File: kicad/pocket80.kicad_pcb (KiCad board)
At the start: 4 copper layers, 68.6 x 107.3 mm, 138 parts, among them J1 USB_C_Receptacle_USB2.0_14P, J2 Conn_02x10_Odd_Even, J3 Conn_01x02, Q1 IRLML6402, Q2 BC847, SW1 F1, SW10 4, SW11 9, SW12 5, SW13 A, SW14 6, SW15 B, SW16 7, SW17 0, SW18 INC, SW19 1, SW2 F2, SW20 DEC, SW21 2, SW22 SEL, SW23 3, SW24 GO!, SW25 SW_Push_DPDT, SW26 RESET, SW3 F3, SW4 F4, SW5 C, SW6 D, SW7 E, SW8 F, SW9 8, U1 Z80CPU, U10 74HC00, U11 74HC138, U12 CH340N, U13 TP4056-42-ESOP8, U14 SX1308, U15 LM393, U16 74HC74, U17 28C256, U2 74HC244, U3 Z80 PIO, U4 Z80 SIO3, U5 Z80 CTC, U6 NE555D, U7 74HC04, U8 62256, U9 24C512, Y1 3.6864M

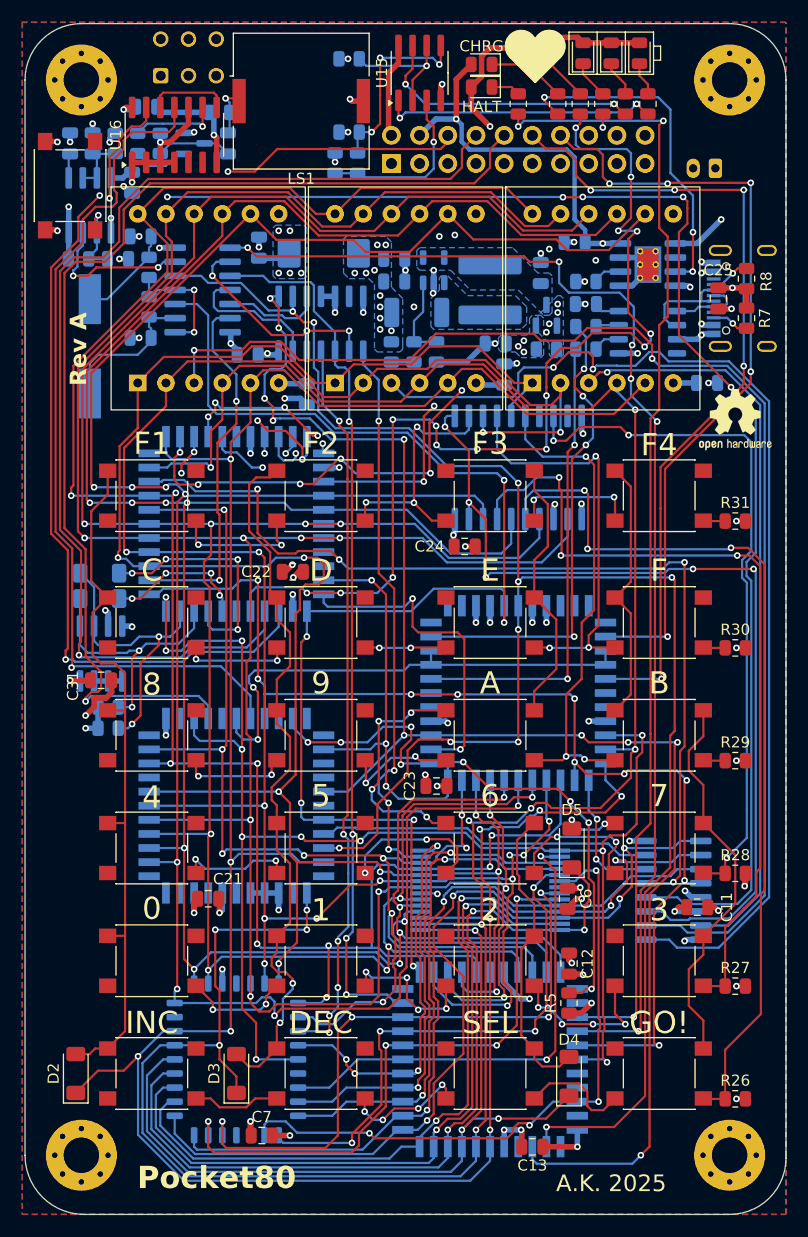
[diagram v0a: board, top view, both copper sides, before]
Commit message: HW: Fix slight mounting hole offset
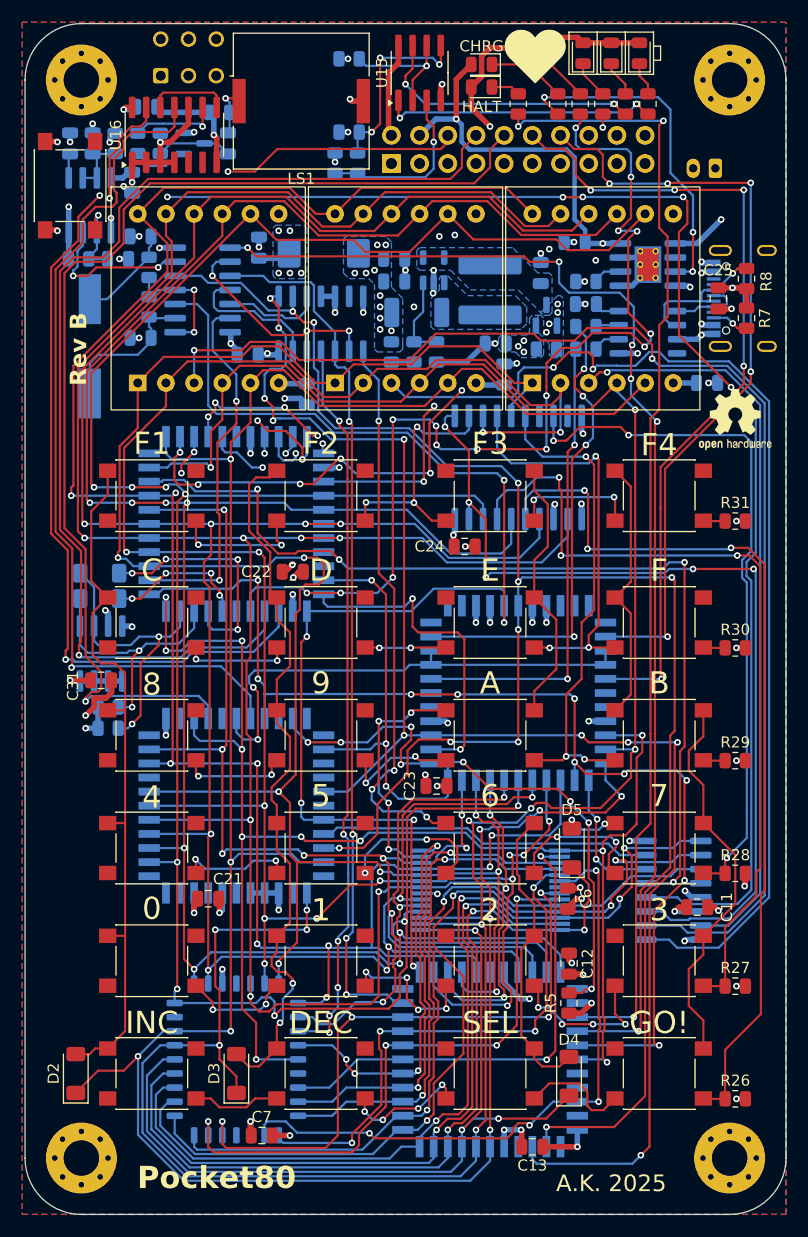
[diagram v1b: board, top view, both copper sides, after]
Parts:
- moved H3 0.25 mm to (160.0, 137.4)
- moved H4 0.25 mm to (101.6, 137.4)
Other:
- outline, holes or cut-outs redrawn
- board text added: "Rev B"
- board text removed: "Rev A"
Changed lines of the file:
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@@
 		(title "Pocket80")
 		(date "2025-10-19")
-		(rev "A")
+		(rev "B")
 		(company "A.K.")
 	)
@@
 	(footprint "MountingHole:MountingHole_3.2mm_M3_Pad_Via"
 		(layer "F.Cu")
-		(at 101.6 137.16)
+		(at 101.6 137.414)
 		(descr "Mounting Hole 3.2mm, M3")
 		(tags "mounting hole 3.2mm m3")
@@
 	(footprint "MountingHole:MountingHole_3.2mm_M3_Pad_Via"
 		(layer "F.Cu")
-		(at 160.02 137.16)
+		(at 160.02 137.414)
 		(descr "Mounting Hole 3.2mm, M3")
 		(tags "mounting hole 3.2mm m3")
@@
 	)
 	(gr_arc
-		(start 101.854 142.494)
-		(mid 98.082292 140.931708)
-		(end 96.52 137.16)
+		(start 101.6 142.494)
+		(mid 98.007898 141.006102)
+		(end 96.52 137.414)
 		(stroke
 			(width 0.05)
@@
 	)
 	(gr_line
-		(start 96.52 137.16)
+		(start 96.52 137.414)
 		(end 96.52 40.259)
 		(stroke
@@
 		(layer "Edge.Cuts")
 	)
-	(gr_line
-		(start 160.019998 142.494)
-		(end 101.854 142.494)
+	(gr_arc
+		(start 165.1 137.414)
+		(mid 163.612102 141.006102)
+		(end 160.02 142.494)
 		(stroke
 			(width 0.05)
@@
 		(layer "Edge.Cuts")
 	)
-	(gr_arc
-		(start 96.52 40.259)
-		(mid 98.007898 36.666898)
-		(end 101.6 35.179)
+	(gr_line
+		(start 160.019998 142.494)
+		(end 101.6 142.494)
 		(stroke
 			(width 0.05)
@@
 	)
 	(gr_arc
-		(start 165.099998 137.414)
-		(mid 163.6121 141.006102)
-		(end 160.019998 142.494)
+		(start 96.52 40.259)
+		(mid 98.007898 36.666898)
+		(end 101.6 35.179)
 		(stroke
 			(width 0.05)
@@
 		)
 	)
-	(gr_text "Rev A"
+	(gr_text "Rev B"
 		(at 101.346 64.516 90)
 		(layer "F.SilkS")

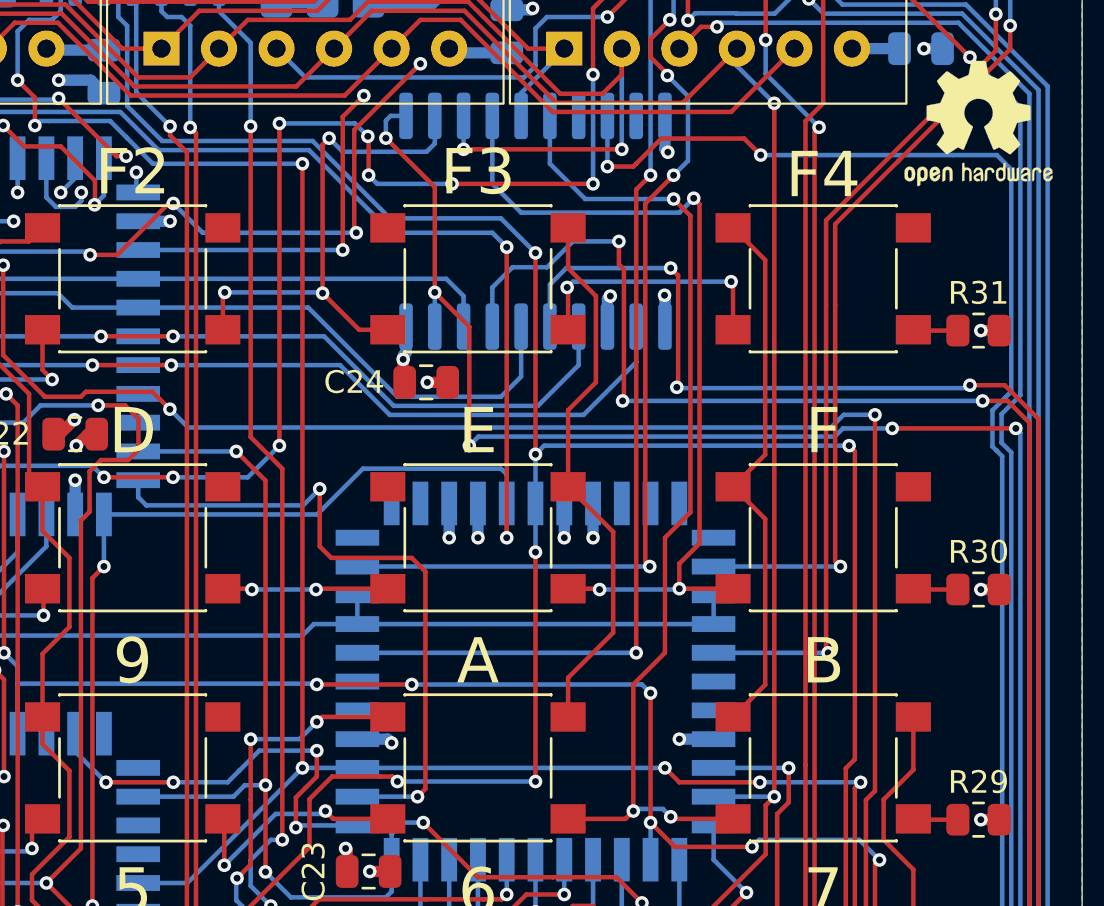
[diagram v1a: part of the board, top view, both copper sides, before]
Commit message: HW: Add pull-ups to the expansion slot inputs
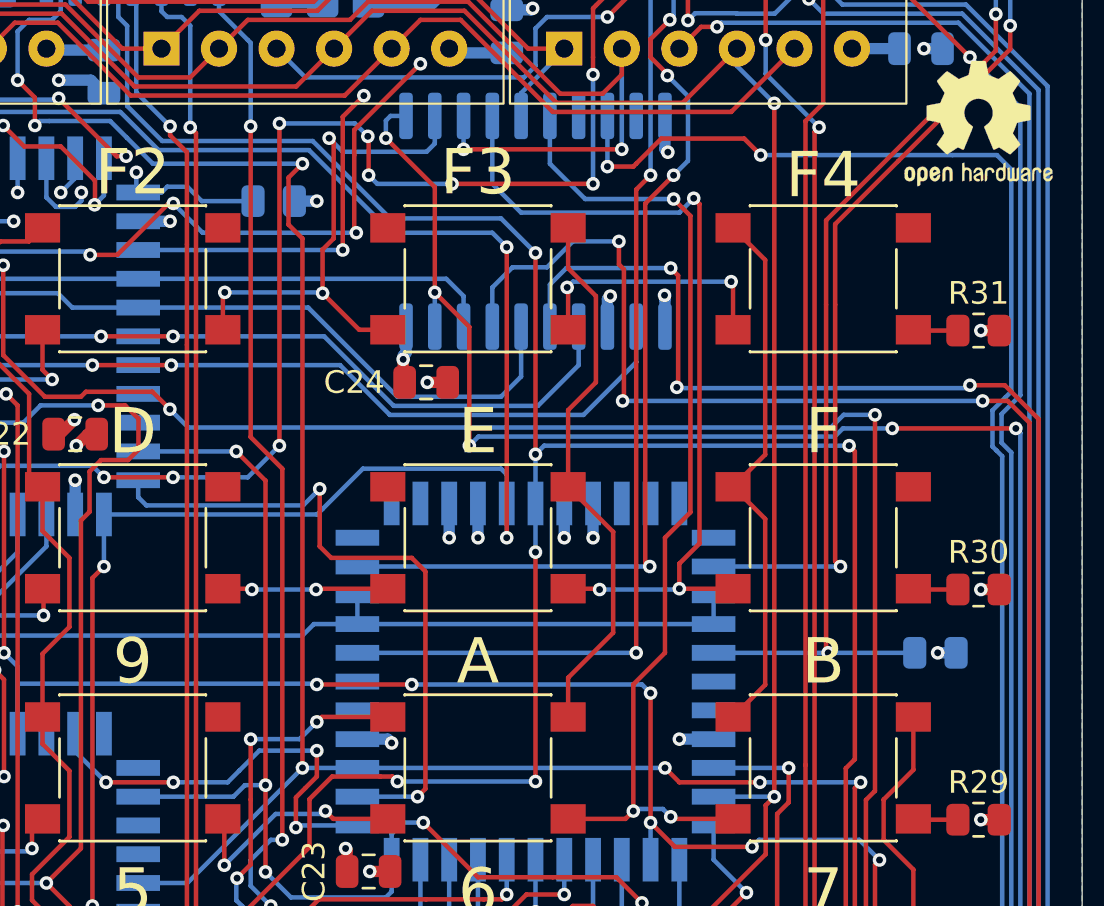
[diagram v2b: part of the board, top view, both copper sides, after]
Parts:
- added R36: 10K, Resistor_SMD:R_0805_2012Metric, B.Cu at (158.6, 94.2)
- added R37: 10K, Resistor_SMD:R_0805_2012Metric, B.Cu at (129.4, 74.3)
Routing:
- net /Expansion/~{ASTB}: track 46.7 -> 52.1 mm
- net /Expansion/TX: track 74.7 -> 78.5 mm
- net VCC: track 119.8 -> 121.6 mm, vias 44 -> 46
- net /CPU/~{M1}: track 137.7 -> 138.2 mm

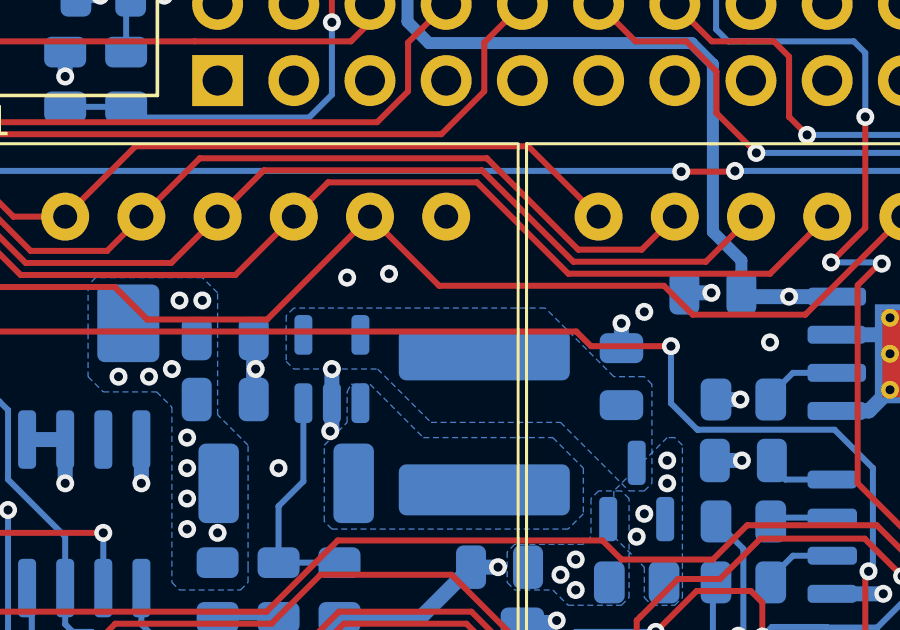
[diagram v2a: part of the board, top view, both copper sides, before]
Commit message: HW: Fix SX1308 footprint TSOT23-5 -> TSOT23-6
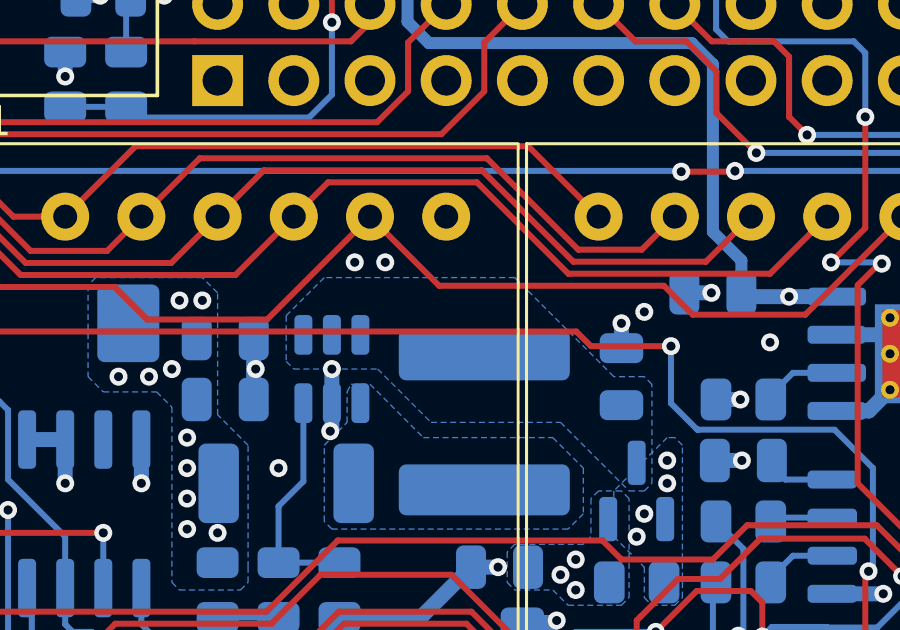
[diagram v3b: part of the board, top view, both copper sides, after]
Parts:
- U14: footprint Package_TO_SOT_SMD:TSOT-23-5 -> Package_TO_SOT_SMD:TSOT-23-6
